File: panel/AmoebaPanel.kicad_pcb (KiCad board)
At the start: 2 copper layers, 92 x 102 mm, 239 parts, among them J1 Conn_01x01_Pin, J2 Conn_01x01_Pin, J3 Conn_01x01_Pin, J4 Conn_01x01_Pin, J5 Conn_01x01_Pin, SW1 SW_SPST

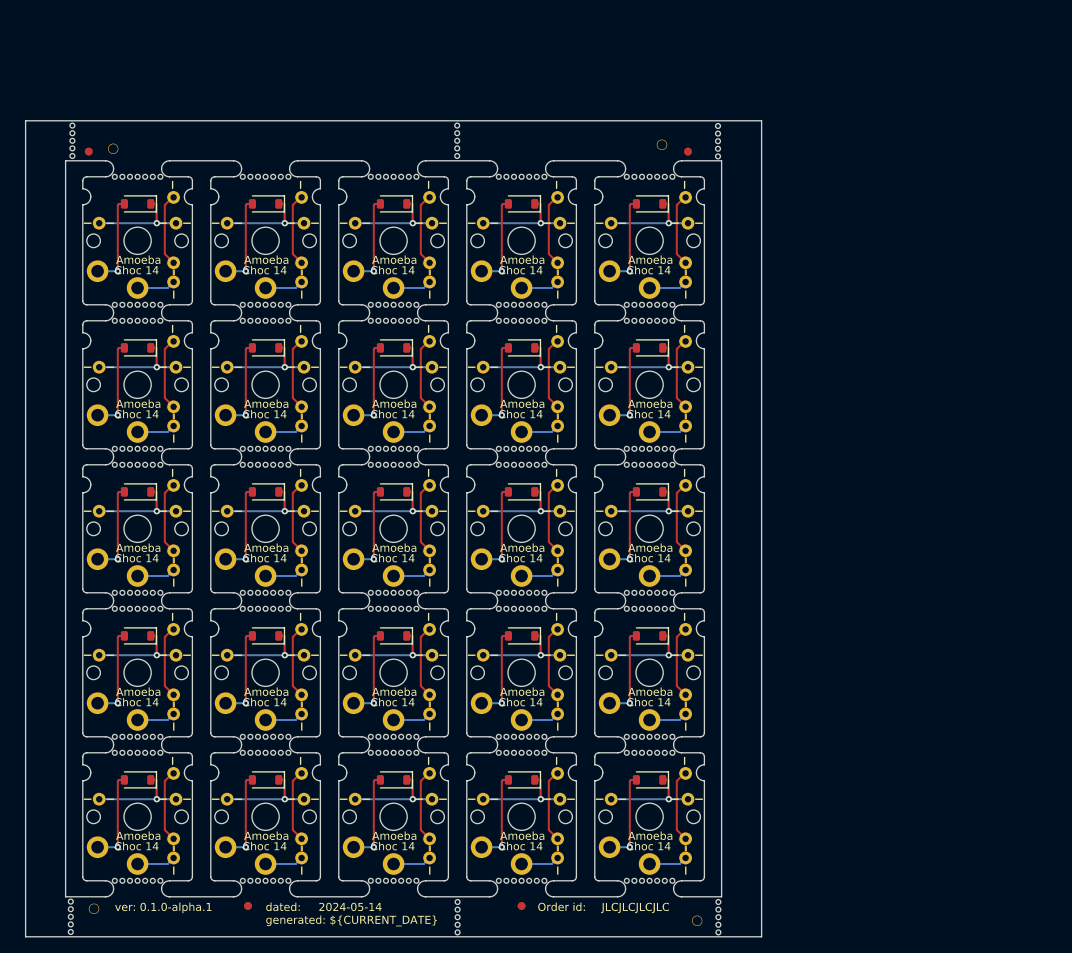
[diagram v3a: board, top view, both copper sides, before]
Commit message: feat(panel): longer bite tabs for breakoff
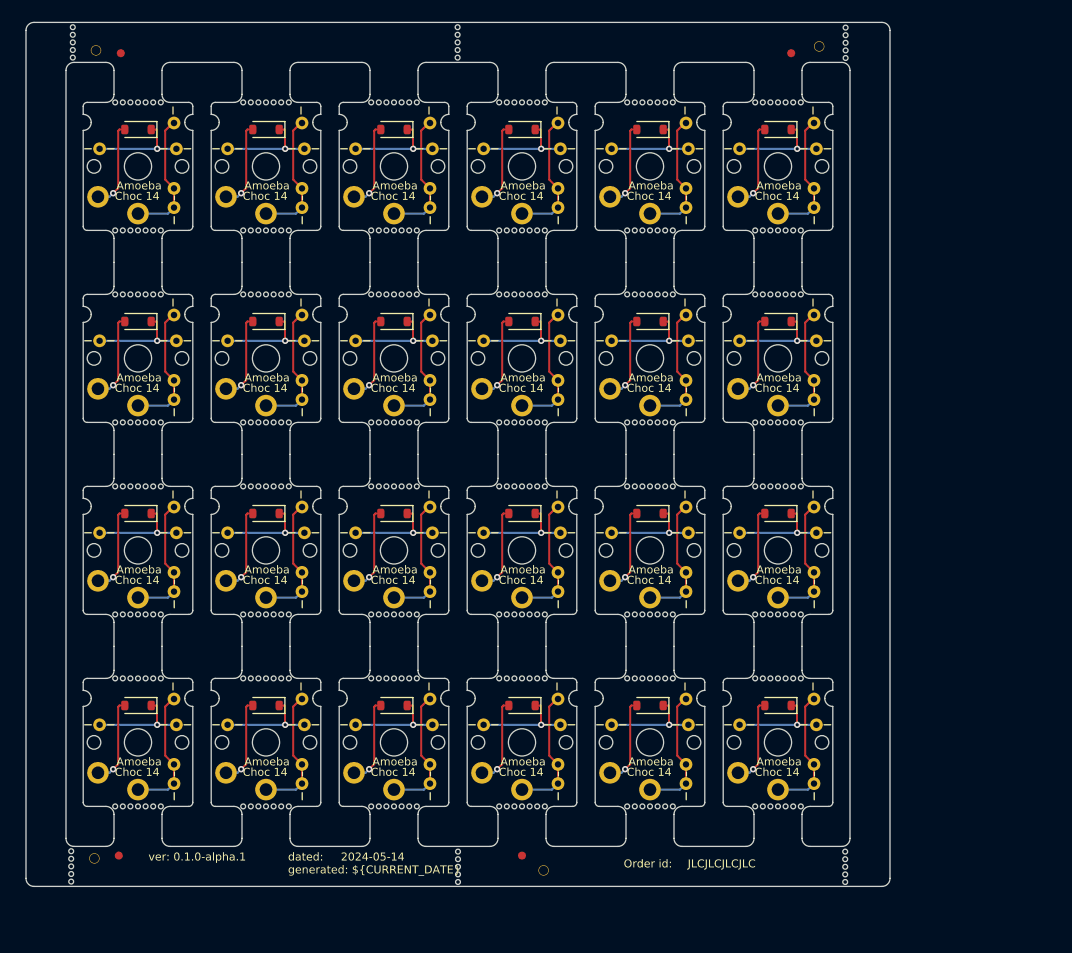
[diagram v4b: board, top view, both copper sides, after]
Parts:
- removed the D1 at (109.2, 127.5)
- removed the D1 at (125.2, 73.5)
- removed the D1 at (109.2, 91.5)
- removed the D1 at (125.2, 109.5)
- removed the D1 at (125.2, 145.5)
- removed the D1 at (157.2, 73.5)
- removed the D1 at (141.2, 73.5)
- removed the D1 at (173.2, 127.5)
- removed the D1 at (109.2, 145.5)
- removed the D1 at (141.2, 91.5)
- removed the D1 at (141.2, 127.5)
- removed the D1 at (141.2, 109.5)
- removed the D1 at (157.2, 145.5)
- removed the D1 at (173.2, 109.5)
- removed the D1 at (109.2, 109.5)
- removed the D1 at (157.2, 91.5)
- removed the D1 at (173.2, 73.5)
- removed the D1 at (125.2, 91.5)
- removed the D1 at (125.2, 127.5)
- removed the D1 at (141.2, 145.5)
- removed the D1 at (109.2, 73.5)
- removed the D1 at (157.2, 109.5)
- removed the D1 at (173.2, 145.5)
- removed the D1 at (173.2, 91.5)
- removed the D1 at (157.2, 127.5)
- removed the J1 at (145.7, 90.7)
- removed the J1 at (113.7, 108.7)
- removed the J1 at (177.7, 126.7)
- removed the J1 at (161.7, 90.7)
- removed the J1 at (145.7, 72.7)
- removed the J1 at (161.7, 72.7)
- removed the J1 at (129.7, 72.7)
- removed the J1 at (145.7, 126.7)
- removed the J1 at (129.7, 144.7)
- removed the J1 at (129.7, 90.7)
- removed the J1 at (145.7, 144.7)
- removed the J1 at (161.7, 108.7)
- removed the J1 at (177.7, 90.7)
- removed the J1 at (177.7, 72.7)
- removed the J1 at (113.7, 126.7)
- removed the J1 at (113.7, 144.7)
- removed the J1 at (113.7, 90.7)
- removed the J1 at (177.7, 108.7)
- removed the J1 at (161.7, 144.7)
- removed the J1 at (113.7, 72.7)
- removed the J1 at (129.7, 126.7)
- removed the J1 at (145.7, 108.7)
- removed the J1 at (177.7, 144.7)
- removed the J1 at (161.7, 126.7)
- removed the J1 at (129.7, 108.7)
- removed the J2 at (161.7, 83.2)
- removed the J2 at (177.7, 101.2)
- removed the J2 at (161.7, 101.2)
- removed the J2 at (129.7, 155.2)
- removed the J2 at (177.7, 119.2)
- removed the J2 at (129.7, 119.2)
- removed the J2 at (145.7, 83.2)
- removed the J2 at (129.7, 83.2)
- removed the J2 at (177.7, 83.2)
- removed the J2 at (129.7, 101.2)
- removed the J2 at (145.7, 101.2)
- removed the J2 at (113.7, 119.2)
- removed the J2 at (113.7, 101.2)
- removed the J2 at (161.7, 119.2)
- removed the J2 at (177.7, 137.2)
- removed the J2 at (145.7, 137.2)
- removed the J2 at (145.7, 119.2)
- removed the J2 at (161.7, 137.2)
- removed the J2 at (161.7, 155.2)
- removed the J2 at (113.7, 83.2)
- removed the J2 at (145.7, 155.2)
- removed the J2 at (113.7, 155.2)
- removed the J2 at (129.7, 137.2)
- removed the J2 at (113.7, 137.2)
- removed the J2 at (177.7, 155.2)
- removed the J3 at (136.4, 129.9)
- removed the J3 at (120.4, 75.9)
- removed the J3 at (104.4, 129.9)
- removed the J3 at (104.4, 111.9)
- removed the J3 at (136.4, 111.9)
- removed the J3 at (104.4, 93.9)
- removed the J3 at (104.4, 147.9)
- removed the J3 at (168.4, 75.9)
- removed the J3 at (168.4, 147.9)
- removed the J3 at (120.4, 129.9)
- removed the J3 at (120.4, 147.9)
- removed the J3 at (136.4, 93.9)
- removed the J3 at (168.4, 129.9)
- removed the J3 at (136.4, 75.9)
- removed the J3 at (152.4, 93.9)
- removed the J3 at (120.4, 111.9)
- removed the J3 at (152.4, 111.9)
- removed the J3 at (136.4, 147.9)
- removed the J3 at (120.4, 93.9)
- removed the J3 at (152.4, 147.9)
- removed the J3 at (152.4, 75.9)
- removed the J3 at (152.4, 129.9)
- removed the J3 at (168.4, 93.9)
- removed the J3 at (104.4, 75.9)
- removed the J3 at (168.4, 111.9)
- removed the J4 at (114.0, 75.9)
- removed the J4 at (114.0, 147.9)
- removed the J4 at (178.0, 111.9)
- removed the J4 at (178.0, 93.9)
- removed the J4 at (130.0, 75.9)
- removed the J4 at (146.0, 75.9)
- removed the J4 at (178.0, 147.9)
- removed the J4 at (130.0, 93.9)
- removed the J4 at (162.0, 129.9)
- removed the J4 at (146.0, 147.9)
- removed the J4 at (130.0, 111.9)
- removed the J4 at (130.0, 147.9)
- removed the J4 at (146.0, 129.9)
- removed the J4 at (178.0, 75.9)
- removed the J4 at (146.0, 111.9)
- removed the J4 at (146.0, 93.9)
- removed the J4 at (114.0, 93.9)
- removed the J4 at (162.0, 93.9)
- removed the J4 at (162.0, 111.9)
- removed the J4 at (162.0, 75.9)
- removed the J4 at (162.0, 147.9)
- removed the J4 at (130.0, 129.9)
- removed the J4 at (114.0, 111.9)
- removed the J4 at (178.0, 129.9)
- removed the J4 at (114.0, 129.9)
- removed the J5 at (145.7, 134.8)
- removed the J5 at (113.7, 98.8)
- removed the J5 at (145.7, 98.8)
- removed the J5 at (113.7, 152.8)
- removed the J5 at (161.7, 134.8)
- removed the J5 at (129.7, 152.8)
- removed the J5 at (177.7, 98.8)
- removed the J5 at (145.7, 80.8)
- removed the J5 at (177.7, 152.8)
- removed the J5 at (129.7, 98.8)
- removed the J5 at (129.7, 134.8)
- removed the J5 at (161.7, 80.8)
- removed the J5 at (177.7, 134.8)
- removed the J5 at (177.7, 116.8)
- removed the J5 at (129.7, 80.8)
- removed the J5 at (161.7, 98.8)
- removed the J5 at (113.7, 80.8)
- removed the J5 at (145.7, 116.8)
- removed the J5 at (129.7, 116.8)
- removed the J5 at (113.7, 116.8)
- removed the J5 at (161.7, 116.8)
- removed the J5 at (177.7, 80.8)
- removed the J5 at (113.7, 134.8)
- removed the J5 at (145.7, 152.8)
- removed the J5 at (161.7, 152.8)
- removed the REF** at (157.2, 106.1)
- removed the REF** at (109.2, 86.1)
- removed the REF** at (173.2, 124.1)
- removed the REF** at (109.2, 104.1)
- removed the REF** at (157.2, 70.1)
- removed the REF** at (109.2, 70.1)
- removed the REF** at (109.2, 122.1)
- removed the REF** at (157.2, 122.1)
- removed the REF** at (109.2, 158.1)
- removed the REF** at (157.2, 88.1)
- removed the REF** at (125.2, 122.1)
- removed the REF** at (125.2, 104.1)
- removed the REF** at (141.2, 140.1)
- removed the REF** at (109.2, 124.1)
- removed the REF** at (157.2, 124.1)
- removed the REF** at (173.2, 158.1)
- removed the REF** at (141.2, 88.1)
- removed the REF** at (141.2, 104.1)
- removed the REF** at (141.2, 106.1)
- removed the REF** at (125.2, 86.1)
- removed the REF** at (141.2, 70.1)
- removed the REF** at (125.2, 140.1)
- removed the REF** at (173.2, 104.1)
- removed the REF** at (173.2, 122.1)
- removed the REF** at (109.2, 142.1)
- removed the REF** at (157.2, 140.1)
- removed the REF** at (157.2, 104.1)
- removed the REF** at (141.2, 122.1)
- removed the REF** at (125.2, 124.1)
- removed the REF** at (125.2, 106.1)
- removed the REF** at (173.2, 86.1)
- removed the REF** at (109.2, 106.1)
- removed the REF** at (141.2, 158.1)
- removed the REF** at (173.2, 70.1)
- removed the REF** at (125.2, 70.1)
- removed the REF** at (157.2, 158.1)
- removed the REF** at (125.2, 158.1)
- removed the REF** at (109.2, 88.1)
- removed the REF** at (173.2, 106.1)
- removed the REF** at (125.2, 142.1)
- removed the REF** at (157.2, 86.1)
- removed the REF** at (141.2, 142.1)
- removed the REF** at (173.2, 88.1)
- removed the REF** at (141.2, 124.1)
- removed the REF** at (141.2, 86.1)
- removed the REF** at (173.2, 140.1)
- removed the REF** at (109.2, 140.1)
- removed the REF** at (173.2, 142.1)
- removed the REF** at (157.2, 142.1)
- removed the REF** at (125.2, 88.1)
- removed the SW1 at (109.2, 78.1)
- removed the SW1 at (173.2, 96.1)
- removed the SW1 at (157.2, 132.1)
- removed the SW1 at (141.2, 114.1)
- removed the SW1 at (157.2, 150.1)
- removed the SW1 at (109.2, 96.1)
- removed the SW1 at (125.2, 132.1)
- removed the SW1 at (157.2, 78.1)
- removed the SW1 at (109.2, 114.1)
- removed the SW1 at (109.2, 150.1)
- removed the SW1 at (173.2, 114.1)
- removed the SW1 at (141.2, 150.1)
- removed the SW1 at (173.2, 78.1)
- removed the SW1 at (125.2, 78.1)
- removed the SW1 at (125.2, 150.1)
- removed the SW1 at (157.2, 96.1)
- removed the SW1 at (141.2, 132.1)
- removed the SW1 at (173.2, 150.1)
- removed the SW1 at (125.2, 114.1)
- removed the SW1 at (173.2, 132.1)
- removed the SW1 at (157.2, 114.1)
- removed the SW1 at (109.2, 132.1)
- removed the SW1 at (141.2, 96.1)
- removed the SW1 at (141.2, 78.1)
- removed the SW1 at (125.2, 96.1)
- added D1: 1N4148, Diode_SMD:D_SOD-123, F.Cu at (109.2, 64.2)
- added D10: 1N4148, Diode_SMD:D_SOD-123, F.Cu at (157.2, 88.2)
- added D11: 1N4148, Diode_SMD:D_SOD-123, F.Cu at (173.2, 88.2)
- added D12: 1N4148, Diode_SMD:D_SOD-123, F.Cu at (189.2, 88.2)
- added D13: 1N4148, Diode_SMD:D_SOD-123, F.Cu at (109.2, 112.2)
- added D14: 1N4148, Diode_SMD:D_SOD-123, F.Cu at (125.2, 112.2)
- added D15: 1N4148, Diode_SMD:D_SOD-123, F.Cu at (141.2, 112.2)
- added D16: 1N4148, Diode_SMD:D_SOD-123, F.Cu at (157.2, 112.2)
- added D17: 1N4148, Diode_SMD:D_SOD-123, F.Cu at (173.2, 112.2)
- added D18: 1N4148, Diode_SMD:D_SOD-123, F.Cu at (189.2, 112.2)
- added D19: 1N4148, Diode_SMD:D_SOD-123, F.Cu at (109.2, 136.2)
- added D2: 1N4148, Diode_SMD:D_SOD-123, F.Cu at (125.2, 64.2)
- added D20: 1N4148, Diode_SMD:D_SOD-123, F.Cu at (125.2, 136.2)
- added D21: 1N4148, Diode_SMD:D_SOD-123, F.Cu at (141.2, 136.2)
- added D22: 1N4148, Diode_SMD:D_SOD-123, F.Cu at (157.2, 136.2)
- added D23: 1N4148, Diode_SMD:D_SOD-123, F.Cu at (173.2, 136.2)
- added D24: 1N4148, Diode_SMD:D_SOD-123, F.Cu at (189.2, 136.2)
- added D3: 1N4148, Diode_SMD:D_SOD-123, F.Cu at (141.2, 64.2)
- added D4: 1N4148, Diode_SMD:D_SOD-123, F.Cu at (157.2, 64.2)
- added D5: 1N4148, Diode_SMD:D_SOD-123, F.Cu at (173.2, 64.2)
- added D6: 1N4148, Diode_SMD:D_SOD-123, F.Cu at (189.2, 64.2)
- added D7: 1N4148, Diode_SMD:D_SOD-123, F.Cu at (109.2, 88.2)
- added D8: 1N4148, Diode_SMD:D_SOD-123, F.Cu at (125.2, 88.2)
- added D9: 1N4148, Diode_SMD:D_SOD-123, F.Cu at (141.2, 88.2)
- added J1: Conn_01x01_Pin, Amoeba_Choc_Nar:Pin_D0.8mm_L7.0mm, B.Cu at (113.8, 63.4)
- added J10: Conn_01x01_Pin, Amoeba_Choc_Nar:Pin_D0.8mm_L7.0mm, B.Cu at (129.8, 71.5)
- added J100: Conn_01x01_Pin, Amoeba_Choc_Nar:Pin_D0.8mm_L7.0mm, B.Cu at (129.8, 143.6)
- added J101: Conn_01x01_Pin, Amoeba_Choc_Nar:Pin_D0.8mm_L7.0mm, B.Cu at (145.8, 135.4)
- added J102: Conn_01x01_Pin, Amoeba_Choc_Nar:Pin_D0.8mm_L7.0mm, B.Cu at (145.8, 145.9)
- added J103: Conn_01x01_Pin, Amoeba_Choc_Nar:Pin_D0.8mm_L7.0mm, B.Cu at (136.4, 138.6)
- added J104: Conn_01x01_Pin, Amoeba_Choc_Nar:Pin_D0.8mm_L7.0mm, B.Cu at (146.1, 138.6)
- added J105: Conn_01x01_Pin, Amoeba_Choc_Nar:Pin_D0.8mm_L7.0mm, B.Cu at (145.8, 143.6)
- added J106: Conn_01x01_Pin, Amoeba_Choc_Nar:Pin_D0.8mm_L7.0mm, B.Cu at (161.8, 135.4)
- added J107: Conn_01x01_Pin, Amoeba_Choc_Nar:Pin_D0.8mm_L7.0mm, B.Cu at (161.8, 145.9)
- added J108: Conn_01x01_Pin, Amoeba_Choc_Nar:Pin_D0.8mm_L7.0mm, B.Cu at (152.4, 138.6)
- added J109: Conn_01x01_Pin, Amoeba_Choc_Nar:Pin_D0.8mm_L7.0mm, B.Cu at (162.1, 138.6)
- added J11: Conn_01x01_Pin, Amoeba_Choc_Nar:Pin_D0.8mm_L7.0mm, B.Cu at (145.8, 63.4)
- added J110: Conn_01x01_Pin, Amoeba_Choc_Nar:Pin_D0.8mm_L7.0mm, B.Cu at (161.8, 143.6)
- added J111: Conn_01x01_Pin, Amoeba_Choc_Nar:Pin_D0.8mm_L7.0mm, B.Cu at (177.8, 135.4)
- added J112: Conn_01x01_Pin, Amoeba_Choc_Nar:Pin_D0.8mm_L7.0mm, B.Cu at (177.8, 145.9)
- added J113: Conn_01x01_Pin, Amoeba_Choc_Nar:Pin_D0.8mm_L7.0mm, B.Cu at (168.4, 138.6)
- added J114: Conn_01x01_Pin, Amoeba_Choc_Nar:Pin_D0.8mm_L7.0mm, B.Cu at (178.1, 138.6)
- added J115: Conn_01x01_Pin, Amoeba_Choc_Nar:Pin_D0.8mm_L7.0mm, B.Cu at (177.8, 143.6)
- added J116: Conn_01x01_Pin, Amoeba_Choc_Nar:Pin_D0.8mm_L7.0mm, B.Cu at (193.8, 135.4)
- added J117: Conn_01x01_Pin, Amoeba_Choc_Nar:Pin_D0.8mm_L7.0mm, B.Cu at (193.8, 145.9)
- added J118: Conn_01x01_Pin, Amoeba_Choc_Nar:Pin_D0.8mm_L7.0mm, B.Cu at (184.4, 138.6)
- added J119: Conn_01x01_Pin, Amoeba_Choc_Nar:Pin_D0.8mm_L7.0mm, B.Cu at (194.1, 138.6)
- added J12: Conn_01x01_Pin, Amoeba_Choc_Nar:Pin_D0.8mm_L7.0mm, B.Cu at (145.8, 74.0)
- added J120: Conn_01x01_Pin, Amoeba_Choc_Nar:Pin_D0.8mm_L7.0mm, B.Cu at (193.8, 143.6)
- added J13: Conn_01x01_Pin, Amoeba_Choc_Nar:Pin_D0.8mm_L7.0mm, B.Cu at (136.4, 66.6)
- added J14: Conn_01x01_Pin, Amoeba_Choc_Nar:Pin_D0.8mm_L7.0mm, B.Cu at (146.1, 66.6)
- added J15: Conn_01x01_Pin, Amoeba_Choc_Nar:Pin_D0.8mm_L7.0mm, B.Cu at (145.8, 71.5)
- added J16: Conn_01x01_Pin, Amoeba_Choc_Nar:Pin_D0.8mm_L7.0mm, B.Cu at (161.8, 63.4)
- added J17: Conn_01x01_Pin, Amoeba_Choc_Nar:Pin_D0.8mm_L7.0mm, B.Cu at (161.8, 74.0)
- added J18: Conn_01x01_Pin, Amoeba_Choc_Nar:Pin_D0.8mm_L7.0mm, B.Cu at (152.4, 66.6)
- added J19: Conn_01x01_Pin, Amoeba_Choc_Nar:Pin_D0.8mm_L7.0mm, B.Cu at (162.1, 66.6)
- added J2: Conn_01x01_Pin, Amoeba_Choc_Nar:Pin_D0.8mm_L7.0mm, B.Cu at (113.8, 74.0)
- added J20: Conn_01x01_Pin, Amoeba_Choc_Nar:Pin_D0.8mm_L7.0mm, B.Cu at (161.8, 71.5)
- added J21: Conn_01x01_Pin, Amoeba_Choc_Nar:Pin_D0.8mm_L7.0mm, B.Cu at (177.8, 63.4)
- added J22: Conn_01x01_Pin, Amoeba_Choc_Nar:Pin_D0.8mm_L7.0mm, B.Cu at (177.8, 74.0)
- added J23: Conn_01x01_Pin, Amoeba_Choc_Nar:Pin_D0.8mm_L7.0mm, B.Cu at (168.4, 66.6)
- added J24: Conn_01x01_Pin, Amoeba_Choc_Nar:Pin_D0.8mm_L7.0mm, B.Cu at (178.1, 66.6)
- added J25: Conn_01x01_Pin, Amoeba_Choc_Nar:Pin_D0.8mm_L7.0mm, B.Cu at (177.8, 71.5)
- added J26: Conn_01x01_Pin, Amoeba_Choc_Nar:Pin_D0.8mm_L7.0mm, B.Cu at (193.8, 63.4)
- added J27: Conn_01x01_Pin, Amoeba_Choc_Nar:Pin_D0.8mm_L7.0mm, B.Cu at (193.8, 74.0)
- added J28: Conn_01x01_Pin, Amoeba_Choc_Nar:Pin_D0.8mm_L7.0mm, B.Cu at (184.4, 66.6)
- added J29: Conn_01x01_Pin, Amoeba_Choc_Nar:Pin_D0.8mm_L7.0mm, B.Cu at (194.1, 66.6)
- added J3: Conn_01x01_Pin, Amoeba_Choc_Nar:Pin_D0.8mm_L7.0mm, B.Cu at (104.5, 66.6)
- added J30: Conn_01x01_Pin, Amoeba_Choc_Nar:Pin_D0.8mm_L7.0mm, B.Cu at (193.8, 71.5)
- added J31: Conn_01x01_Pin, Amoeba_Choc_Nar:Pin_D0.8mm_L7.0mm, B.Cu at (113.8, 87.4)
- added J32: Conn_01x01_Pin, Amoeba_Choc_Nar:Pin_D0.8mm_L7.0mm, B.Cu at (113.8, 98.0)
- added J33: Conn_01x01_Pin, Amoeba_Choc_Nar:Pin_D0.8mm_L7.0mm, B.Cu at (104.5, 90.6)
- added J34: Conn_01x01_Pin, Amoeba_Choc_Nar:Pin_D0.8mm_L7.0mm, B.Cu at (114.0, 90.6)
- added J35: Conn_01x01_Pin, Amoeba_Choc_Nar:Pin_D0.8mm_L7.0mm, B.Cu at (113.8, 95.5)
- added J36: Conn_01x01_Pin, Amoeba_Choc_Nar:Pin_D0.8mm_L7.0mm, B.Cu at (129.8, 87.4)
- added J37: Conn_01x01_Pin, Amoeba_Choc_Nar:Pin_D0.8mm_L7.0mm, B.Cu at (129.8, 98.0)
- added J38: Conn_01x01_Pin, Amoeba_Choc_Nar:Pin_D0.8mm_L7.0mm, B.Cu at (120.5, 90.6)
- added J39: Conn_01x01_Pin, Amoeba_Choc_Nar:Pin_D0.8mm_L7.0mm, B.Cu at (130.1, 90.6)
- added J4: Conn_01x01_Pin, Amoeba_Choc_Nar:Pin_D0.8mm_L7.0mm, B.Cu at (114.0, 66.6)
- added J40: Conn_01x01_Pin, Amoeba_Choc_Nar:Pin_D0.8mm_L7.0mm, B.Cu at (129.8, 95.5)
- added J41: Conn_01x01_Pin, Amoeba_Choc_Nar:Pin_D0.8mm_L7.0mm, B.Cu at (145.8, 87.4)
- added J42: Conn_01x01_Pin, Amoeba_Choc_Nar:Pin_D0.8mm_L7.0mm, B.Cu at (145.8, 98.0)
- added J43: Conn_01x01_Pin, Amoeba_Choc_Nar:Pin_D0.8mm_L7.0mm, B.Cu at (136.4, 90.6)
- added J44: Conn_01x01_Pin, Amoeba_Choc_Nar:Pin_D0.8mm_L7.0mm, B.Cu at (146.1, 90.6)
- added J45: Conn_01x01_Pin, Amoeba_Choc_Nar:Pin_D0.8mm_L7.0mm, B.Cu at (145.8, 95.5)
- added J46: Conn_01x01_Pin, Amoeba_Choc_Nar:Pin_D0.8mm_L7.0mm, B.Cu at (161.8, 87.4)
- added J47: Conn_01x01_Pin, Amoeba_Choc_Nar:Pin_D0.8mm_L7.0mm, B.Cu at (161.8, 98.0)
- added J48: Conn_01x01_Pin, Amoeba_Choc_Nar:Pin_D0.8mm_L7.0mm, B.Cu at (152.4, 90.6)
- added J49: Conn_01x01_Pin, Amoeba_Choc_Nar:Pin_D0.8mm_L7.0mm, B.Cu at (162.1, 90.6)
- added J5: Conn_01x01_Pin, Amoeba_Choc_Nar:Pin_D0.8mm_L7.0mm, B.Cu at (113.8, 71.5)
- added J50: Conn_01x01_Pin, Amoeba_Choc_Nar:Pin_D0.8mm_L7.0mm, B.Cu at (161.8, 95.5)
- added J51: Conn_01x01_Pin, Amoeba_Choc_Nar:Pin_D0.8mm_L7.0mm, B.Cu at (177.8, 87.4)
- added J52: Conn_01x01_Pin, Amoeba_Choc_Nar:Pin_D0.8mm_L7.0mm, B.Cu at (177.8, 98.0)
- added J53: Conn_01x01_Pin, Amoeba_Choc_Nar:Pin_D0.8mm_L7.0mm, B.Cu at (168.4, 90.6)
- added J54: Conn_01x01_Pin, Amoeba_Choc_Nar:Pin_D0.8mm_L7.0mm, B.Cu at (178.1, 90.6)
- added J55: Conn_01x01_Pin, Amoeba_Choc_Nar:Pin_D0.8mm_L7.0mm, B.Cu at (177.8, 95.5)
- added J56: Conn_01x01_Pin, Amoeba_Choc_Nar:Pin_D0.8mm_L7.0mm, B.Cu at (193.8, 87.4)
- added J57: Conn_01x01_Pin, Amoeba_Choc_Nar:Pin_D0.8mm_L7.0mm, B.Cu at (193.8, 98.0)
- added J58: Conn_01x01_Pin, Amoeba_Choc_Nar:Pin_D0.8mm_L7.0mm, B.Cu at (184.4, 90.6)
- added J59: Conn_01x01_Pin, Amoeba_Choc_Nar:Pin_D0.8mm_L7.0mm, B.Cu at (194.1, 90.6)
- added J6: Conn_01x01_Pin, Amoeba_Choc_Nar:Pin_D0.8mm_L7.0mm, B.Cu at (129.8, 63.4)
- added J60: Conn_01x01_Pin, Amoeba_Choc_Nar:Pin_D0.8mm_L7.0mm, B.Cu at (193.8, 95.5)
- added J61: Conn_01x01_Pin, Amoeba_Choc_Nar:Pin_D0.8mm_L7.0mm, B.Cu at (113.8, 111.4)
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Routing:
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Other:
- board size 92 x 102 mm -> 108 x 108 mm
- board text added: "v010a1"

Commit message: feat(panel): update for SOD-323
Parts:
- removed the D1 at (109.2, 64.2)
- removed D10, D11, D12, D13, D14, D15, D16, D17, D18, D19, D2, D20, D21, D22, D23, D24, D3, D4, D5, D6, D7, D8, D9: 1N4148, Diode_SMD:D_SOD-123
- removed J10, J100, J101, J102, J103, J104, J105, J106, J107, J108, J109, J11, J110, J111, J112, J113, J114, J115, J116, J117, J118, J119, J12, J120, J13, J14, J15, J16, J17, J18, J19, J20, J21, J22, J23, J24, J25, J26, J27, J28, J29, J30, J31, J32, J33, J34, J35, J36, J37, J38, J39, J40, J41, J42, J43, J44, J45, J46, J47, J48, J49, J50, J51, J52, J53, J54, J55, J56, J57, J58, J59, J6, J60, J61, J62, J63, J64, J65, J66, J67, J68, J69, J7, J70, J71, J72, J73, J74, J75, J76, J77, J78, J79, J8, J80, J81, J82, J83, J84, J85, J86, J87, J88, J89, J9, J90, J91, J92, J93, J94, J95, J96, J97, J98, J99: Conn_01x01_Pin, Amoeba_Choc_Nar:Pin_D0.8mm_L7.0mm
- removed REF**1, REF**10, REF**11, REF**12, REF**13, REF**14, REF**15, REF**16, REF**17, REF**18, REF**19, REF**2, REF**20, REF**21, REF**22, REF**23, REF**24, REF**25, REF**26, REF**27, REF**28, REF**29, REF**3, REF**30, REF**31, REF**32, REF**33, REF**34, REF**35, REF**36, REF**37, REF**38, REF**39, REF**4, REF**40, REF**41, REF**42, REF**43, REF**44, REF**45, REF**46, REF**5, REF**6, REF**7, REF**8, REF**9: Mouse_Bites, Amoeba_Choc_Nar:Mouse_Bites
- removed SW10, SW11, SW12, SW13, SW14, SW15, SW16, SW17, SW18, SW19, SW2, SW20, SW21, SW22, SW23, SW24, SW3, SW4, SW5, SW6, SW7, SW8, SW9: SW_SPST, Amoeba_Choc_Nar:pg1350-hotswap
- added D1: 1N4148, Diode_SMD:D_SOD-323_HandSoldering, F.Cu at (141.2, 88.2)
- added D1: 1N4148, Diode_SMD:D_SOD-323_HandSoldering, F.Cu at (109.2, 136.2)
- added D1: 1N4148, Diode_SMD:D_SOD-323_HandSoldering, F.Cu at (109.2, 64.2)
- added D1: 1N4148, Diode_SMD:D_SOD-323_HandSoldering, F.Cu at (157.2, 136.2)
- added D1: 1N4148, Diode_SMD:D_SOD-323_HandSoldering, F.Cu at (109.2, 112.2)
- added D1: 1N4148, Diode_SMD:D_SOD-323_HandSoldering, F.Cu at (141.2, 64.2)
- added D1: 1N4148, Diode_SMD:D_SOD-323_HandSoldering, F.Cu at (125.2, 64.2)
- added D1: 1N4148, Diode_SMD:D_SOD-323_HandSoldering, F.Cu at (173.2, 136.2)
- added D1: 1N4148, Diode_SMD:D_SOD-323_HandSoldering, F.Cu at (125.2, 112.2)
- added D1: 1N4148, Diode_SMD:D_SOD-323_HandSoldering, F.Cu at (173.2, 112.2)
- added D1: 1N4148, Diode_SMD:D_SOD-323_HandSoldering, F.Cu at (189.2, 112.2)
- added D1: 1N4148, Diode_SMD:D_SOD-323_HandSoldering, F.Cu at (157.2, 88.2)
- added D1: 1N4148, Diode_SMD:D_SOD-323_HandSoldering, F.Cu at (141.2, 136.2)
- added D1: 1N4148, Diode_SMD:D_SOD-323_HandSoldering, F.Cu at (189.2, 88.2)
- added D1: 1N4148, Diode_SMD:D_SOD-323_HandSoldering, F.Cu at (109.2, 88.2)
- added D1: 1N4148, Diode_SMD:D_SOD-323_HandSoldering, F.Cu at (125.2, 88.2)
- added D1: 1N4148, Diode_SMD:D_SOD-323_HandSoldering, F.Cu at (157.2, 112.2)
- added D1: 1N4148, Diode_SMD:D_SOD-323_HandSoldering, F.Cu at (125.2, 136.2)
- added D1: 1N4148, Diode_SMD:D_SOD-323_HandSoldering, F.Cu at (189.2, 136.2)
- added D1: 1N4148, Diode_SMD:D_SOD-323_HandSoldering, F.Cu at (173.2, 64.2)
- added D1: 1N4148, Diode_SMD:D_SOD-323_HandSoldering, F.Cu at (141.2, 112.2)
- added D1: 1N4148, Diode_SMD:D_SOD-323_HandSoldering, F.Cu at (173.2, 88.2)
- added D1: 1N4148, Diode_SMD:D_SOD-323_HandSoldering, F.Cu at (189.2, 64.2)
- added D1: 1N4148, Diode_SMD:D_SOD-323_HandSoldering, F.Cu at (157.2, 64.2)
- added J1: Conn_01x01_Pin, Amoeba_Choc_Nar:Pin_D0.8mm_L7.0mm, B.Cu at (177.8, 87.4)
- added J1: Conn_01x01_Pin, Amoeba_Choc_Nar:Pin_D0.8mm_L7.0mm, B.Cu at (177.8, 63.4)
- added J1: Conn_01x01_Pin, Amoeba_Choc_Nar:Pin_D0.8mm_L7.0mm, B.Cu at (193.8, 135.4)
- added J1: Conn_01x01_Pin, Amoeba_Choc_Nar:Pin_D0.8mm_L7.0mm, B.Cu at (129.8, 87.4)
- added J1: Conn_01x01_Pin, Amoeba_Choc_Nar:Pin_D0.8mm_L7.0mm, B.Cu at (161.8, 63.4)
- added J1: Conn_01x01_Pin, Amoeba_Choc_Nar:Pin_D0.8mm_L7.0mm, B.Cu at (145.8, 135.4)
- added J1: Conn_01x01_Pin, Amoeba_Choc_Nar:Pin_D0.8mm_L7.0mm, B.Cu at (145.8, 111.4)
- added J1: Conn_01x01_Pin, Amoeba_Choc_Nar:Pin_D0.8mm_L7.0mm, B.Cu at (129.8, 111.4)
- added J1: Conn_01x01_Pin, Amoeba_Choc_Nar:Pin_D0.8mm_L7.0mm, B.Cu at (129.8, 63.4)
- added J1: Conn_01x01_Pin, Amoeba_Choc_Nar:Pin_D0.8mm_L7.0mm, B.Cu at (113.8, 135.4)
- added J1: Conn_01x01_Pin, Amoeba_Choc_Nar:Pin_D0.8mm_L7.0mm, B.Cu at (193.8, 63.4)
- added J1: Conn_01x01_Pin, Amoeba_Choc_Nar:Pin_D0.8mm_L7.0mm, B.Cu at (161.8, 135.4)
- added J1: Conn_01x01_Pin, Amoeba_Choc_Nar:Pin_D0.8mm_L7.0mm, B.Cu at (177.8, 111.4)
- added J1: Conn_01x01_Pin, Amoeba_Choc_Nar:Pin_D0.8mm_L7.0mm, B.Cu at (113.8, 111.4)
- added J1: Conn_01x01_Pin, Amoeba_Choc_Nar:Pin_D0.8mm_L7.0mm, B.Cu at (129.8, 135.4)
- added J1: Conn_01x01_Pin, Amoeba_Choc_Nar:Pin_D0.8mm_L7.0mm, B.Cu at (145.8, 63.4)
- added J1: Conn_01x01_Pin, Amoeba_Choc_Nar:Pin_D0.8mm_L7.0mm, B.Cu at (193.8, 111.4)
- added J1: Conn_01x01_Pin, Amoeba_Choc_Nar:Pin_D0.8mm_L7.0mm, B.Cu at (113.8, 87.4)
- added J1: Conn_01x01_Pin, Amoeba_Choc_Nar:Pin_D0.8mm_L7.0mm, B.Cu at (161.8, 111.4)
- added J1: Conn_01x01_Pin, Amoeba_Choc_Nar:Pin_D0.8mm_L7.0mm, B.Cu at (193.8, 87.4)
- added J1: Conn_01x01_Pin, Amoeba_Choc_Nar:Pin_D0.8mm_L7.0mm, B.Cu at (177.8, 135.4)
- added J1: Conn_01x01_Pin, Amoeba_Choc_Nar:Pin_D0.8mm_L7.0mm, B.Cu at (145.8, 87.4)
- added J1: Conn_01x01_Pin, Amoeba_Choc_Nar:Pin_D0.8mm_L7.0mm, B.Cu at (161.8, 87.4)
- added J2: Conn_01x01_Pin, Amoeba_Choc_Nar:Pin_D0.8mm_L7.0mm, B.Cu at (145.8, 145.9)
- added J2: Conn_01x01_Pin, Amoeba_Choc_Nar:Pin_D0.8mm_L7.0mm, B.Cu at (145.8, 74.0)
- added J2: Conn_01x01_Pin, Amoeba_Choc_Nar:Pin_D0.8mm_L7.0mm, B.Cu at (161.8, 74.0)
- added J2: Conn_01x01_Pin, Amoeba_Choc_Nar:Pin_D0.8mm_L7.0mm, B.Cu at (177.8, 122.0)
- added J2: Conn_01x01_Pin, Amoeba_Choc_Nar:Pin_D0.8mm_L7.0mm, B.Cu at (113.8, 122.0)
- added J2: Conn_01x01_Pin, Amoeba_Choc_Nar:Pin_D0.8mm_L7.0mm, B.Cu at (193.8, 98.0)
- added J2: Conn_01x01_Pin, Amoeba_Choc_Nar:Pin_D0.8mm_L7.0mm, B.Cu at (161.8, 145.9)
- added J2: Conn_01x01_Pin, Amoeba_Choc_Nar:Pin_D0.8mm_L7.0mm, B.Cu at (193.8, 122.0)
- added J2: Conn_01x01_Pin, Amoeba_Choc_Nar:Pin_D0.8mm_L7.0mm, B.Cu at (177.8, 98.0)
- added J2: Conn_01x01_Pin, Amoeba_Choc_Nar:Pin_D0.8mm_L7.0mm, B.Cu at (113.8, 145.9)
- added J2: Conn_01x01_Pin, Amoeba_Choc_Nar:Pin_D0.8mm_L7.0mm, B.Cu at (113.8, 98.0)
- added J2: Conn_01x01_Pin, Amoeba_Choc_Nar:Pin_D0.8mm_L7.0mm, B.Cu at (129.8, 74.0)
- added J2: Conn_01x01_Pin, Amoeba_Choc_Nar:Pin_D0.8mm_L7.0mm, B.Cu at (177.8, 145.9)
- added J2: Conn_01x01_Pin, Amoeba_Choc_Nar:Pin_D0.8mm_L7.0mm, B.Cu at (161.8, 98.0)
- added J2: Conn_01x01_Pin, Amoeba_Choc_Nar:Pin_D0.8mm_L7.0mm, B.Cu at (129.8, 145.9)
- added J2: Conn_01x01_Pin, Amoeba_Choc_Nar:Pin_D0.8mm_L7.0mm, B.Cu at (161.8, 122.0)
- added J2: Conn_01x01_Pin, Amoeba_Choc_Nar:Pin_D0.8mm_L7.0mm, B.Cu at (193.8, 74.0)
- added J2: Conn_01x01_Pin, Amoeba_Choc_Nar:Pin_D0.8mm_L7.0mm, B.Cu at (129.8, 122.0)
- added J2: Conn_01x01_Pin, Amoeba_Choc_Nar:Pin_D0.8mm_L7.0mm, B.Cu at (145.8, 122.0)
- added J2: Conn_01x01_Pin, Amoeba_Choc_Nar:Pin_D0.8mm_L7.0mm, B.Cu at (145.8, 98.0)
- added J2: Conn_01x01_Pin, Amoeba_Choc_Nar:Pin_D0.8mm_L7.0mm, B.Cu at (177.8, 74.0)
- added J2: Conn_01x01_Pin, Amoeba_Choc_Nar:Pin_D0.8mm_L7.0mm, B.Cu at (193.8, 145.9)
- added J2: Conn_01x01_Pin, Amoeba_Choc_Nar:Pin_D0.8mm_L7.0mm, B.Cu at (129.8, 98.0)
- added J3: Conn_01x01_Pin, Amoeba_Choc_Nar:Pin_D0.8mm_L7.0mm, B.Cu at (104.5, 90.6)
- added J3: Conn_01x01_Pin, Amoeba_Choc_Nar:Pin_D0.8mm_L7.0mm, B.Cu at (136.4, 90.6)
- added J3: Conn_01x01_Pin, Amoeba_Choc_Nar:Pin_D0.8mm_L7.0mm, B.Cu at (120.5, 138.6)
- added J3: Conn_01x01_Pin, Amoeba_Choc_Nar:Pin_D0.8mm_L7.0mm, B.Cu at (168.4, 114.6)
- added J3: Conn_01x01_Pin, Amoeba_Choc_Nar:Pin_D0.8mm_L7.0mm, B.Cu at (136.4, 66.6)
- added J3: Conn_01x01_Pin, Amoeba_Choc_Nar:Pin_D0.8mm_L7.0mm, B.Cu at (184.4, 138.6)
- added J3: Conn_01x01_Pin, Amoeba_Choc_Nar:Pin_D0.8mm_L7.0mm, B.Cu at (168.4, 66.6)
- added J3: Conn_01x01_Pin, Amoeba_Choc_Nar:Pin_D0.8mm_L7.0mm, B.Cu at (152.4, 90.6)
- added J3: Conn_01x01_Pin, Amoeba_Choc_Nar:Pin_D0.8mm_L7.0mm, B.Cu at (120.5, 114.6)
- added J3: Conn_01x01_Pin, Amoeba_Choc_Nar:Pin_D0.8mm_L7.0mm, B.Cu at (136.4, 114.6)
- added J3: Conn_01x01_Pin, Amoeba_Choc_Nar:Pin_D0.8mm_L7.0mm, B.Cu at (152.4, 66.6)
- added J3: Conn_01x01_Pin, Amoeba_Choc_Nar:Pin_D0.8mm_L7.0mm, B.Cu at (152.4, 114.6)
- added J3: Conn_01x01_Pin, Amoeba_Choc_Nar:Pin_D0.8mm_L7.0mm, B.Cu at (184.4, 90.6)
- added J3: Conn_01x01_Pin, Amoeba_Choc_Nar:Pin_D0.8mm_L7.0mm, B.Cu at (104.5, 114.6)
- added J3: Conn_01x01_Pin, Amoeba_Choc_Nar:Pin_D0.8mm_L7.0mm, B.Cu at (168.4, 138.6)
- added J3: Conn_01x01_Pin, Amoeba_Choc_Nar:Pin_D0.8mm_L7.0mm, B.Cu at (120.5, 90.6)
- added J3: Conn_01x01_Pin, Amoeba_Choc_Nar:Pin_D0.8mm_L7.0mm, B.Cu at (104.5, 138.6)
- added J3: Conn_01x01_Pin, Amoeba_Choc_Nar:Pin_D0.8mm_L7.0mm, B.Cu at (184.4, 66.6)
- added J3: Conn_01x01_Pin, Amoeba_Choc_Nar:Pin_D0.8mm_L7.0mm, B.Cu at (184.4, 114.6)
- added J3: Conn_01x01_Pin, Amoeba_Choc_Nar:Pin_D0.8mm_L7.0mm, B.Cu at (168.4, 90.6)
- added J3: Conn_01x01_Pin, Amoeba_Choc_Nar:Pin_D0.8mm_L7.0mm, B.Cu at (136.4, 138.6)
- added J3: Conn_01x01_Pin, Amoeba_Choc_Nar:Pin_D0.8mm_L7.0mm, B.Cu at (120.5, 66.6)
- added J3: Conn_01x01_Pin, Amoeba_Choc_Nar:Pin_D0.8mm_L7.0mm, B.Cu at (152.4, 138.6)
- added J4: Conn_01x01_Pin, Amoeba_Choc_Nar:Pin_D0.8mm_L7.0mm, B.Cu at (130.1, 114.6)
- added J4: Conn_01x01_Pin, Amoeba_Choc_Nar:Pin_D0.8mm_L7.0mm, B.Cu at (194.1, 90.6)
- added J4: Conn_01x01_Pin, Amoeba_Choc_Nar:Pin_D0.8mm_L7.0mm, B.Cu at (178.1, 138.6)
- added J4: Conn_01x01_Pin, Amoeba_Choc_Nar:Pin_D0.8mm_L7.0mm, B.Cu at (178.1, 66.6)
- added J4: Conn_01x01_Pin, Amoeba_Choc_Nar:Pin_D0.8mm_L7.0mm, B.Cu at (130.1, 90.6)
- added J4: Conn_01x01_Pin, Amoeba_Choc_Nar:Pin_D0.8mm_L7.0mm, B.Cu at (178.1, 114.6)
- added J4: Conn_01x01_Pin, Amoeba_Choc_Nar:Pin_D0.8mm_L7.0mm, B.Cu at (162.1, 138.6)
- added J4: Conn_01x01_Pin, Amoeba_Choc_Nar:Pin_D0.8mm_L7.0mm, B.Cu at (162.1, 114.6)
- added J4: Conn_01x01_Pin, Amoeba_Choc_Nar:Pin_D0.8mm_L7.0mm, B.Cu at (146.1, 66.6)
- added J4: Conn_01x01_Pin, Amoeba_Choc_Nar:Pin_D0.8mm_L7.0mm, B.Cu at (114.0, 138.6)
- added J4: Conn_01x01_Pin, Amoeba_Choc_Nar:Pin_D0.8mm_L7.0mm, B.Cu at (114.0, 90.6)
- added J4: Conn_01x01_Pin, Amoeba_Choc_Nar:Pin_D0.8mm_L7.0mm, B.Cu at (114.0, 114.6)
- added J4: Conn_01x01_Pin, Amoeba_Choc_Nar:Pin_D0.8mm_L7.0mm, B.Cu at (162.1, 66.6)
- added J4: Conn_01x01_Pin, Amoeba_Choc_Nar:Pin_D0.8mm_L7.0mm, B.Cu at (194.1, 114.6)
- added J4: Conn_01x01_Pin, Amoeba_Choc_Nar:Pin_D0.8mm_L7.0mm, B.Cu at (194.1, 138.6)
- added J4: Conn_01x01_Pin, Amoeba_Choc_Nar:Pin_D0.8mm_L7.0mm, B.Cu at (146.1, 114.6)
- added J4: Conn_01x01_Pin, Amoeba_Choc_Nar:Pin_D0.8mm_L7.0mm, B.Cu at (130.1, 138.6)
- added J4: Conn_01x01_Pin, Amoeba_Choc_Nar:Pin_D0.8mm_L7.0mm, B.Cu at (146.1, 90.6)
- added J4: Conn_01x01_Pin, Amoeba_Choc_Nar:Pin_D0.8mm_L7.0mm, B.Cu at (146.1, 138.6)
- added J4: Conn_01x01_Pin, Amoeba_Choc_Nar:Pin_D0.8mm_L7.0mm, B.Cu at (194.1, 66.6)
- added J4: Conn_01x01_Pin, Amoeba_Choc_Nar:Pin_D0.8mm_L7.0mm, B.Cu at (178.1, 90.6)
- added J4: Conn_01x01_Pin, Amoeba_Choc_Nar:Pin_D0.8mm_L7.0mm, B.Cu at (130.1, 66.6)
- added J4: Conn_01x01_Pin, Amoeba_Choc_Nar:Pin_D0.8mm_L7.0mm, B.Cu at (162.1, 90.6)
- added J5: Conn_01x01_Pin, Amoeba_Choc_Nar:Pin_D0.8mm_L7.0mm, B.Cu at (161.8, 119.5)
- added J5: Conn_01x01_Pin, Amoeba_Choc_Nar:Pin_D0.8mm_L7.0mm, B.Cu at (193.8, 119.5)
- added J5: Conn_01x01_Pin, Amoeba_Choc_Nar:Pin_D0.8mm_L7.0mm, B.Cu at (193.8, 71.5)
- added J5: Conn_01x01_Pin, Amoeba_Choc_Nar:Pin_D0.8mm_L7.0mm, B.Cu at (161.8, 71.5)
- added J5: Conn_01x01_Pin, Amoeba_Choc_Nar:Pin_D0.8mm_L7.0mm, B.Cu at (177.8, 71.5)
- added J5: Conn_01x01_Pin, Amoeba_Choc_Nar:Pin_D0.8mm_L7.0mm, B.Cu at (129.8, 71.5)
- added J5: Conn_01x01_Pin, Amoeba_Choc_Nar:Pin_D0.8mm_L7.0mm, B.Cu at (145.8, 119.5)
- added J5: Conn_01x01_Pin, Amoeba_Choc_Nar:Pin_D0.8mm_L7.0mm, B.Cu at (113.8, 119.5)
- added J5: Conn_01x01_Pin, Amoeba_Choc_Nar:Pin_D0.8mm_L7.0mm, B.Cu at (129.8, 95.5)
- added J5: Conn_01x01_Pin, Amoeba_Choc_Nar:Pin_D0.8mm_L7.0mm, B.Cu at (113.8, 95.5)
- added J5: Conn_01x01_Pin, Amoeba_Choc_Nar:Pin_D0.8mm_L7.0mm, B.Cu at (145.8, 143.6)
- added J5: Conn_01x01_Pin, Amoeba_Choc_Nar:Pin_D0.8mm_L7.0mm, B.Cu at (129.8, 119.5)
- added J5: Conn_01x01_Pin, Amoeba_Choc_Nar:Pin_D0.8mm_L7.0mm, B.Cu at (129.8, 143.6)
- added J5: Conn_01x01_Pin, Amoeba_Choc_Nar:Pin_D0.8mm_L7.0mm, B.Cu at (177.8, 143.6)
- added J5: Conn_01x01_Pin, Amoeba_Choc_Nar:Pin_D0.8mm_L7.0mm, B.Cu at (161.8, 95.5)
- added J5: Conn_01x01_Pin, Amoeba_Choc_Nar:Pin_D0.8mm_L7.0mm, B.Cu at (113.8, 143.6)
- added J5: Conn_01x01_Pin, Amoeba_Choc_Nar:Pin_D0.8mm_L7.0mm, B.Cu at (177.8, 95.5)
- added J5: Conn_01x01_Pin, Amoeba_Choc_Nar:Pin_D0.8mm_L7.0mm, B.Cu at (145.8, 71.5)
- added J5: Conn_01x01_Pin, Amoeba_Choc_Nar:Pin_D0.8mm_L7.0mm, B.Cu at (161.8, 143.6)
- added J5: Conn_01x01_Pin, Amoeba_Choc_Nar:Pin_D0.8mm_L7.0mm, B.Cu at (145.8, 95.5)
- added J5: Conn_01x01_Pin, Amoeba_Choc_Nar:Pin_D0.8mm_L7.0mm, B.Cu at (177.8, 119.5)
- added J5: Conn_01x01_Pin, Amoeba_Choc_Nar:Pin_D0.8mm_L7.0mm, B.Cu at (193.8, 143.6)
- added J5: Conn_01x01_Pin, Amoeba_Choc_Nar:Pin_D0.8mm_L7.0mm, B.Cu at (193.8, 95.5)
- added REF**: Mouse_Bites, Amoeba_Choc_Nar:Mouse_Bites, F.Cu at (141.2, 76.8)
- added REF**: Mouse_Bites, Amoeba_Choc_Nar:Mouse_Bites, F.Cu at (157.2, 132.8)
- added REF**: Mouse_Bites, Amoeba_Choc_Nar:Mouse_Bites, F.Cu at (125.2, 148.8)
- added REF**: Mouse_Bites, Amoeba_Choc_Nar:Mouse_Bites, F.Cu at (173.2, 100.8)
- added REF**: Mouse_Bites, Amoeba_Choc_Nar:Mouse_Bites, F.Cu at (173.2, 76.8)
- added REF**: Mouse_Bites, Amoeba_Choc_Nar:Mouse_Bites, F.Cu at (125.2, 60.8)
- added REF**: Mouse_Bites, Amoeba_Choc_Nar:Mouse_Bites, F.Cu at (141.2, 60.8)
- added REF**: Mouse_Bites, Amoeba_Choc_Nar:Mouse_Bites, F.Cu at (141.2, 108.8)
- added REF**: Mouse_Bites, Amoeba_Choc_Nar:Mouse_Bites, F.Cu at (157.2, 148.8)
- added REF**: Mouse_Bites, Amoeba_Choc_Nar:Mouse_Bites, F.Cu at (109.2, 148.8)
- added REF**: Mouse_Bites, Amoeba_Choc_Nar:Mouse_Bites, F.Cu at (141.2, 132.8)
- added REF**: Mouse_Bites, Amoeba_Choc_Nar:Mouse_Bites, F.Cu at (125.2, 108.8)
- added REF**: Mouse_Bites, Amoeba_Choc_Nar:Mouse_Bites, F.Cu at (189.2, 108.8)
- added REF**: Mouse_Bites, Amoeba_Choc_Nar:Mouse_Bites, F.Cu at (189.2, 84.8)
- added REF**: Mouse_Bites, Amoeba_Choc_Nar:Mouse_Bites, F.Cu at (141.2, 84.8)
- added REF**: Mouse_Bites, Amoeba_Choc_Nar:Mouse_Bites, F.Cu at (109.2, 84.8)
- added REF**: Mouse_Bites, Amoeba_Choc_Nar:Mouse_Bites, F.Cu at (125.2, 76.8)
- added REF**: Mouse_Bites, Amoeba_Choc_Nar:Mouse_Bites, F.Cu at (189.2, 76.8)
- added REF**: Mouse_Bites, Amoeba_Choc_Nar:Mouse_Bites, F.Cu at (157.2, 108.8)
- added REF**: Mouse_Bites, Amoeba_Choc_Nar:Mouse_Bites, F.Cu at (141.2, 124.8)
- added REF**: Mouse_Bites, Amoeba_Choc_Nar:Mouse_Bites, F.Cu at (173.2, 108.8)
- added REF**: Mouse_Bites, Amoeba_Choc_Nar:Mouse_Bites, F.Cu at (157.2, 100.8)
- added REF**: Mouse_Bites, Amoeba_Choc_Nar:Mouse_Bites, F.Cu at (125.2, 124.8)
- added REF**: Mouse_Bites, Amoeba_Choc_Nar:Mouse_Bites, F.Cu at (173.2, 132.8)
- added REF**: Mouse_Bites, Amoeba_Choc_Nar:Mouse_Bites, F.Cu at (189.2, 124.8)
- added REF**: Mouse_Bites, Amoeba_Choc_Nar:Mouse_Bites, F.Cu at (125.2, 100.8)
- added REF**: Mouse_Bites, Amoeba_Choc_Nar:Mouse_Bites, F.Cu at (189.2, 132.8)
- added REF**: Mouse_Bites, Amoeba_Choc_Nar:Mouse_Bites, F.Cu at (157.2, 84.8)
- added REF**: Mouse_Bites, Amoeba_Choc_Nar:Mouse_Bites, F.Cu at (173.2, 148.8)
- added REF**: Mouse_Bites, Amoeba_Choc_Nar:Mouse_Bites, F.Cu at (157.2, 60.8)
- added REF**: Mouse_Bites, Amoeba_Choc_Nar:Mouse_Bites, F.Cu at (141.2, 100.8)
- added REF**: Mouse_Bites, Amoeba_Choc_Nar:Mouse_Bites, F.Cu at (157.2, 76.8)
- added REF**: Mouse_Bites, Amoeba_Choc_Nar:Mouse_Bites, F.Cu at (109.2, 132.8)
- added REF**: Mouse_Bites, Amoeba_Choc_Nar:Mouse_Bites, F.Cu at (189.2, 60.8)
- added REF**: Mouse_Bites, Amoeba_Choc_Nar:Mouse_Bites, F.Cu at (109.2, 108.8)
- added REF**: Mouse_Bites, Amoeba_Choc_Nar:Mouse_Bites, F.Cu at (125.2, 84.8)
- added REF**: Mouse_Bites, Amoeba_Choc_Nar:Mouse_Bites, F.Cu at (157.2, 124.8)
- added REF**: Mouse_Bites, Amoeba_Choc_Nar:Mouse_Bites, F.Cu at (173.2, 84.8)
- added REF**: Mouse_Bites, Amoeba_Choc_Nar:Mouse_Bites, F.Cu at (141.2, 148.8)
- added REF**: Mouse_Bites, Amoeba_Choc_Nar:Mouse_Bites, F.Cu at (109.2, 100.8)
- added REF**: Mouse_Bites, Amoeba_Choc_Nar:Mouse_Bites, F.Cu at (125.2, 132.8)
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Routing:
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
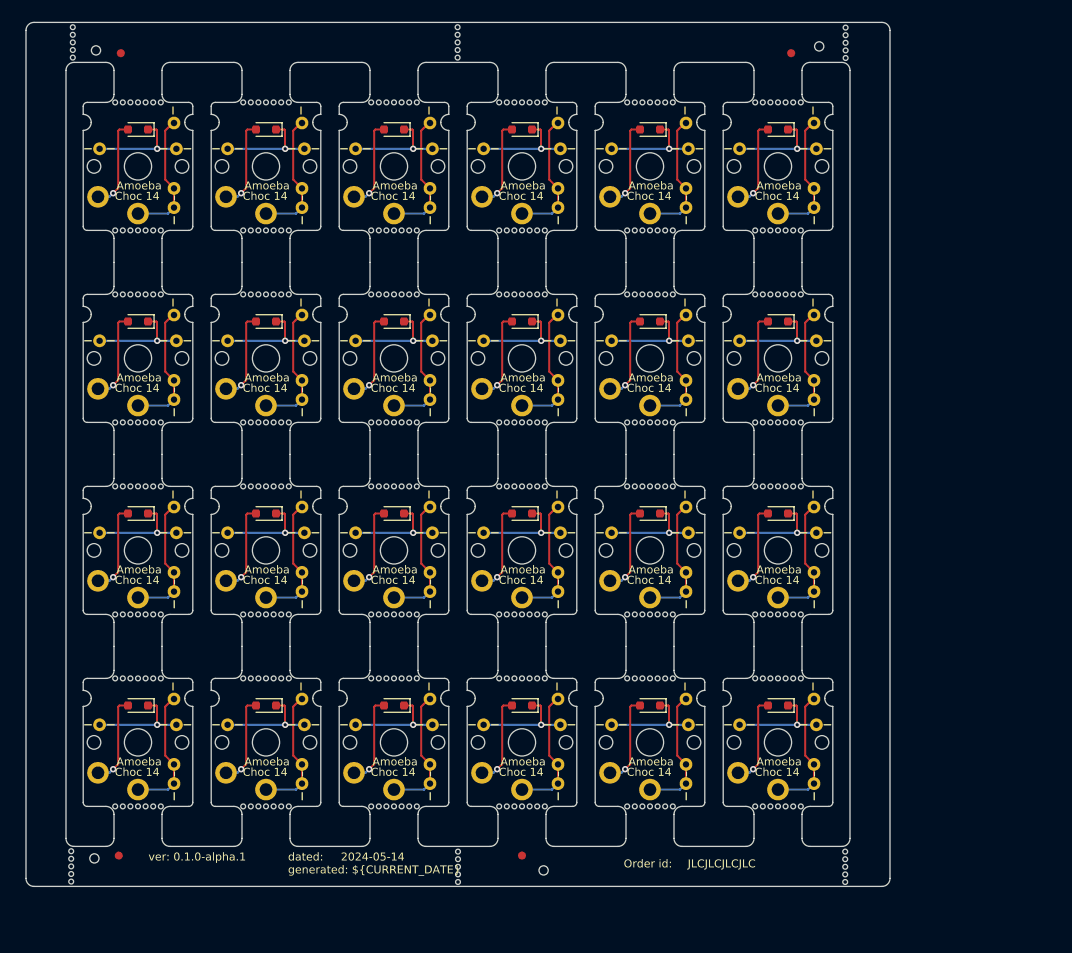
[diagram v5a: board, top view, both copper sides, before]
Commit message: feat(panel): tidy up tooling holes and silk
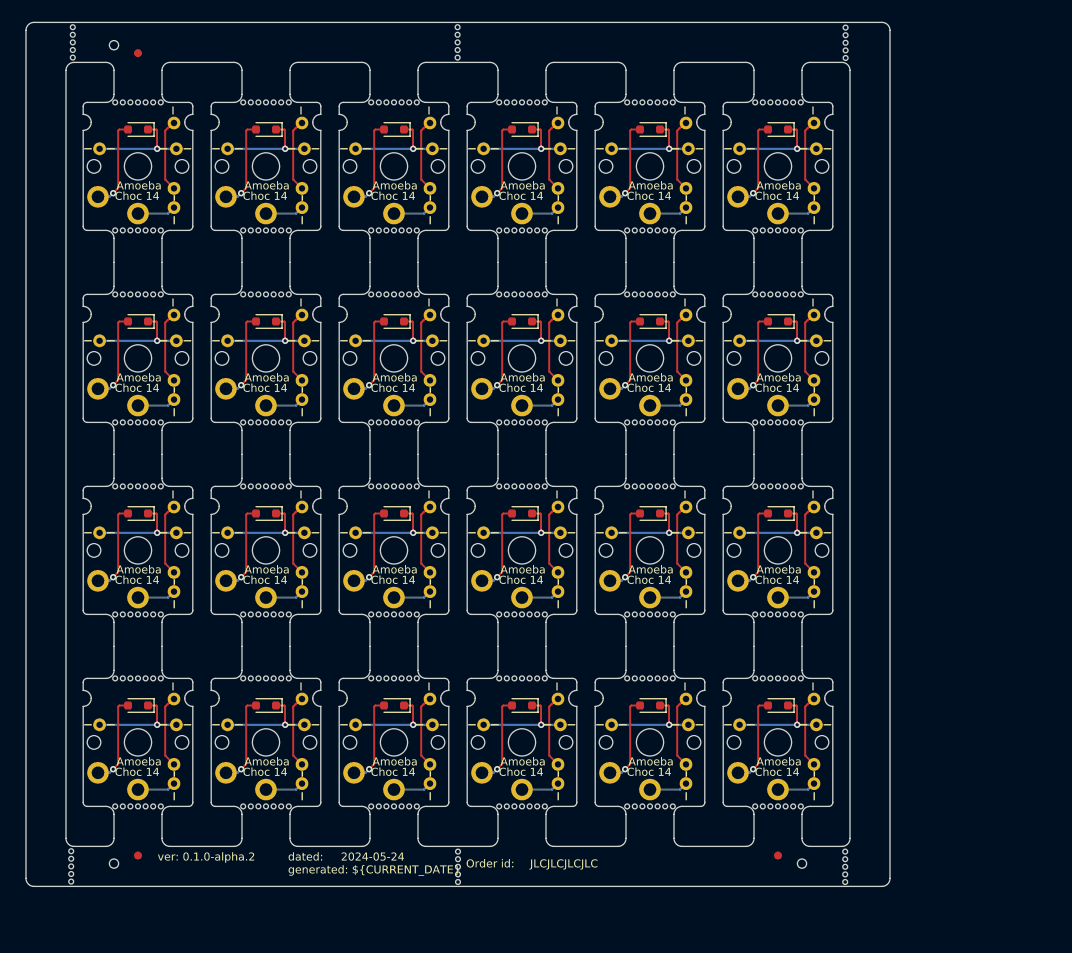
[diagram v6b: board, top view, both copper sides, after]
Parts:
- removed the ? at (194.4, 53.8)
- removed the REF** at (190.9, 54.6)
- moved ? 32.3 mm to (192.2, 155.9)
- moved REF** 32.0 mm to (189.2, 154.9)
- moved ? 2.53 mm to (106.2, 155.9)
- moved REF** 2.40 mm to (109.2, 154.9)
- moved ? 2.34 mm to (106.2, 53.6)
- moved REF** 2.15 mm to (109.2, 54.6)
